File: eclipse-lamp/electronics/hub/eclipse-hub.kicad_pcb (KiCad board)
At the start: 2 copper layers, 36 x 36 mm, 42 parts, among them J1 TO CORE J2

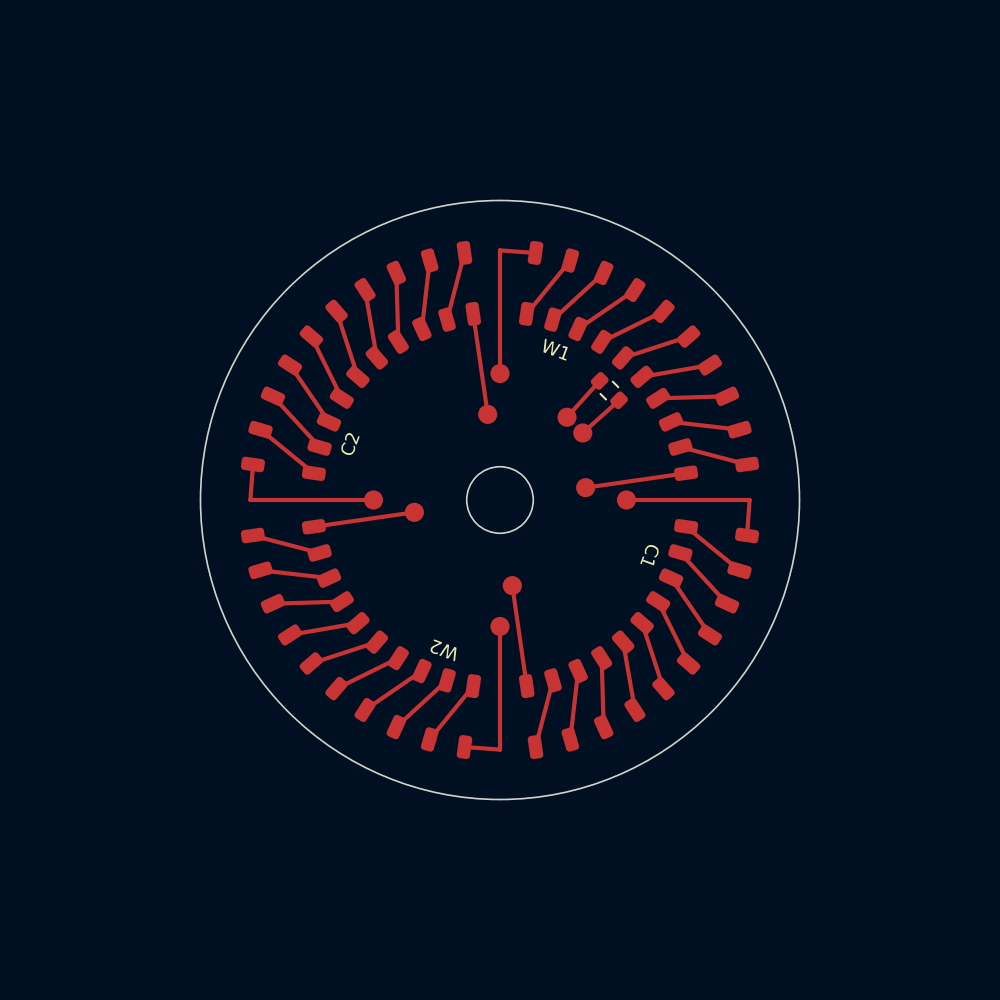
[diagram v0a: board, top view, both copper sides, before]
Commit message: ECLIPSE Tree: thick glowing trunk, 5x crown, fibre-lit samaras, hub light engine
- Tree: 44 mm cast-bronze trunk shell around a PMMA light-guide core with
  glowing bark fissures, 6 buttress roots, D68 burl, 73 branches + 1222 spur
  twigs, 657 end-glow fibre tips with diffusing samaras
- Hub: D56 two-sided light engine (8 LEDs into the trunk core, 8 into the
  fibre bundles) as the first series element of each 100 mA chain; core
  board circuit unchanged; ERC/DRC/parity clean, all schematics wired
- Renders: fissure-glow bark shader, samaras, trunk close-up; BOM, docs

Co-Authored-By: Claude Opus 5.5 <noreply@anthropic.com>
Claude-Session: https://claude.ai/code/session_01UC4Dpjx8nsVkJqTcucsgsg
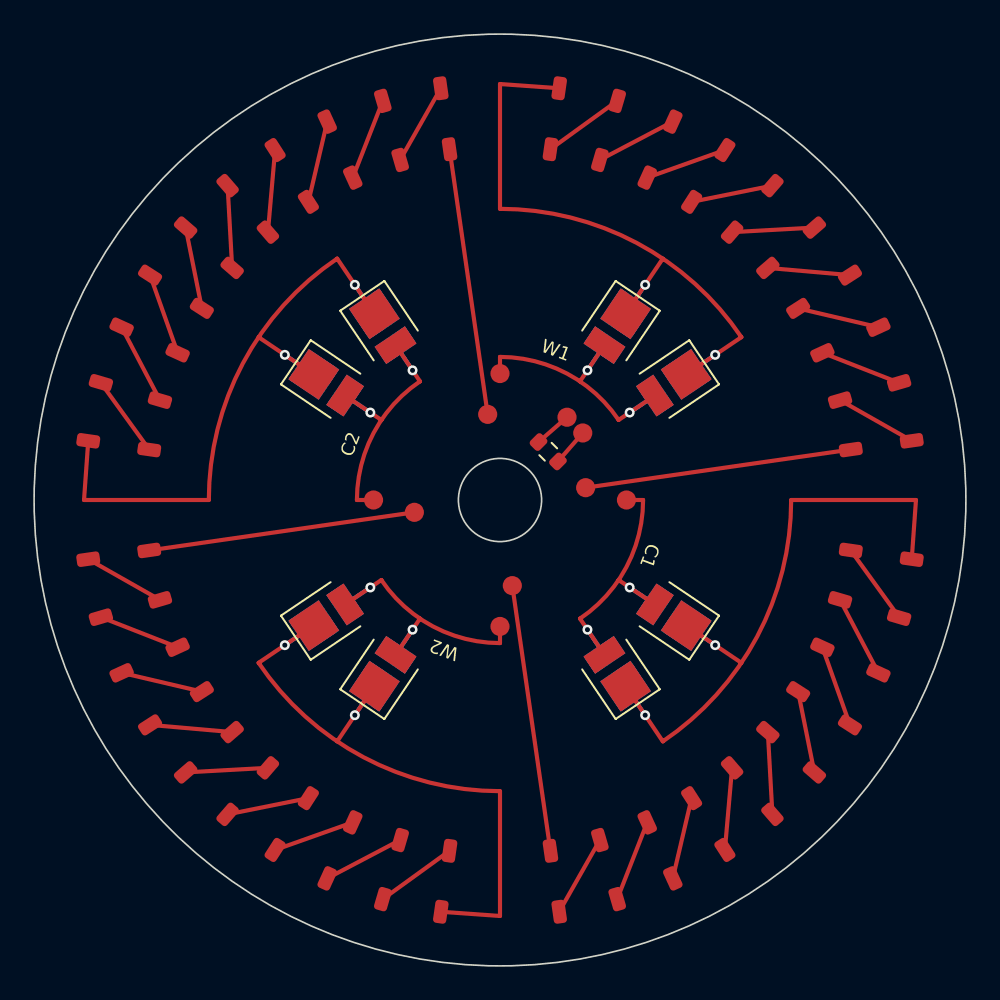
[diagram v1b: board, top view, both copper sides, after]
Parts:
- added D1: 2700K, LED_SMD:LED_PLCC_2835, F.Cu at (157.0, 139.6)
- added D10: 2700K, LED_SMD:LED_PLCC_2835, F.Cu at (139.6, 157.0)
- added D11: 2700K, LED_SMD:LED_PLCC_2835, B.Cu at (143.0, 160.4)
- added D12: 2700K, LED_SMD:LED_PLCC_2835, B.Cu at (139.6, 157.0)
- added D13: 6500K, LED_SMD:LED_PLCC_2835, F.Cu at (139.6, 143.0)
- added D14: 6500K, LED_SMD:LED_PLCC_2835, F.Cu at (143.0, 139.6)
- added D15: 6500K, LED_SMD:LED_PLCC_2835, B.Cu at (139.6, 143.0)
- added D16: 6500K, LED_SMD:LED_PLCC_2835, B.Cu at (143.0, 139.6)
- added D2: 2700K, LED_SMD:LED_PLCC_2835, F.Cu at (160.4, 143.0)
- added D3: 2700K, LED_SMD:LED_PLCC_2835, B.Cu at (157.0, 139.6)
- added D4: 2700K, LED_SMD:LED_PLCC_2835, B.Cu at (160.4, 143.0)
- added D5: 6500K, LED_SMD:LED_PLCC_2835, F.Cu at (160.4, 157.0)
- added D6: 6500K, LED_SMD:LED_PLCC_2835, F.Cu at (157.0, 160.4)
- added D7: 6500K, LED_SMD:LED_PLCC_2835, B.Cu at (160.4, 157.0)
- added D8: 6500K, LED_SMD:LED_PLCC_2835, B.Cu at (157.0, 160.4)
- added D9: 2700K, LED_SMD:LED_PLCC_2835, F.Cu at (143.0, 160.4)
- moved S1 10.0 mm to (153.3, 127.1)
- moved S10 10.0 mm to (172.9, 146.7)
- moved S11 10.0 mm to (172.9, 153.3)
- moved S20 10.0 mm to (153.3, 172.9)
- moved S21 10.0 mm to (146.7, 172.9)
- moved S30 10.0 mm to (127.1, 153.3)
- moved S31 10.0 mm to (127.1, 146.7)
- moved S40 10.0 mm to (146.7, 127.1)
- moved S14 10.0 mm to (169.5, 162.5)
- moved S17 10.0 mm to (162.5, 169.5)
- moved S24 10.0 mm to (137.5, 169.5)
- moved S7 10.0 mm to (169.5, 137.5)
- moved S27 10.0 mm to (130.5, 162.5)
- moved S34 10.0 mm to (130.5, 137.5)
- moved S37 10.0 mm to (137.5, 130.5)
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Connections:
- J1 pad 2: Net-(J1-Pin_2) -> Net-(D5-A)
- J1 pad 3: Net-(J1-Pin_3) -> Net-(D1-A)
- J1 pad 8: Net-(J1-Pin_8) -> Net-(D10-A)
- J1 pad 9: Net-(J1-Pin_9) -> Net-(D13-A)
- S1 pad 1: Net-(J1-Pin_3) -> Net-(D1-K)
- S11 pad 1: Net-(J1-Pin_2) -> Net-(D5-K)
- S21 pad 1: Net-(J1-Pin_8) -> Net-(D10-K)
- S31 pad 1: Net-(J1-Pin_9) -> Net-(D13-K)
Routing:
- net Net-(D10-K): track 0.00 -> 40.2 mm, vias 0 -> 2
- net Net-(D13-K): track 0.00 -> 40.2 mm, vias 0 -> 2
- net Net-(D5-K): track 0.00 -> 40.2 mm, vias 0 -> 2
- net Net-(D1-K): track 0.00 -> 40.2 mm, vias 0 -> 2
- net Net-(D10-A): track 0.00 -> 18.2 mm, vias 0 -> 2
- net Net-(D13-A): track 0.00 -> 18.2 mm, vias 0 -> 2
- net Net-(D5-A): track 0.00 -> 18.2 mm, vias 0 -> 2
- net Net-(D1-A): track 0.00 -> 18.2 mm, vias 0 -> 2
- net Net-(J1-Pin_7): track 6.10 -> 16.1 mm
- net Net-(J1-Pin_10): track 6.10 -> 16.1 mm
- net Net-(J1-Pin_1): track 6.10 -> 16.1 mm
- net Net-(J1-Pin_4): track 6.10 -> 16.1 mm
- net Net-(J1-Pin_8): track 9.54 -> 0.00 mm
- net Net-(J1-Pin_9): track 9.54 -> 0.00 mm
- net Net-(J1-Pin_2): track 9.54 -> 0.00 mm
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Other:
- board size 36 x 36 mm -> 56 x 56 mm
